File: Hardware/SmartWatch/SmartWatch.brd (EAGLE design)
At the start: 36.8 x 40.6 mm, 79 parts, among them U1 STM32L476, U10 MICRO-USB, U11 BNO055, U3 UG-2828GDEDF11, U4 FAN5331SX, U5 APDS-9960, U6 MCP73831, U7 AP2112K-3.3TRG-1, U8 ASDK-32.768, U9 ASCO-8

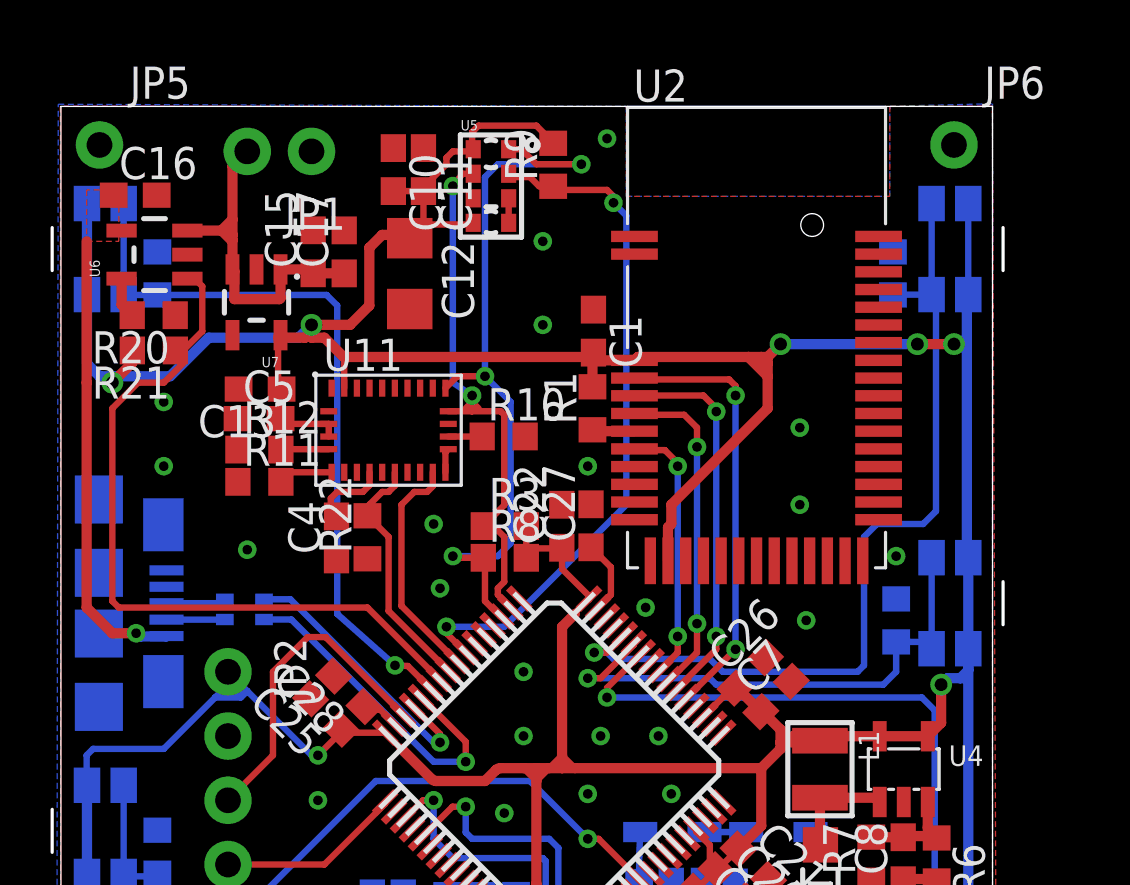
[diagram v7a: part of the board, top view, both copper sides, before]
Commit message: added test points and icreased keepout around bluetooth
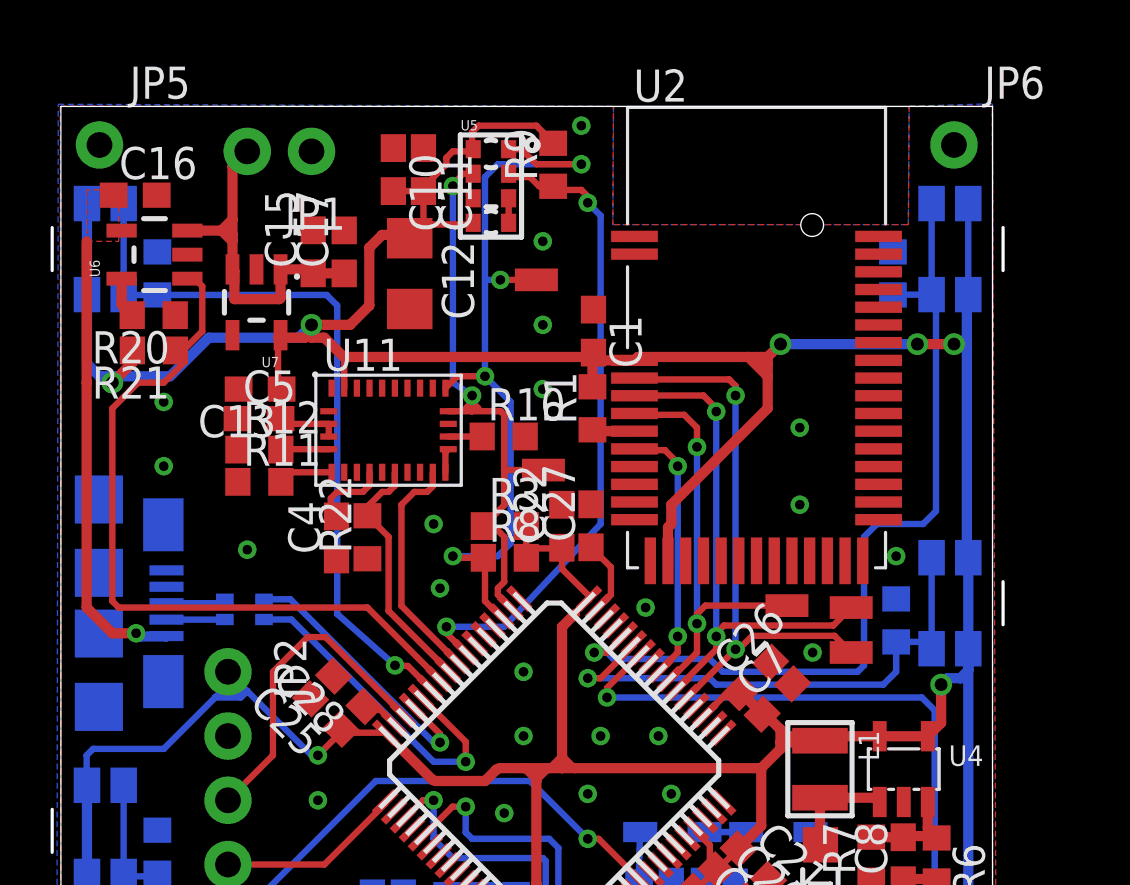
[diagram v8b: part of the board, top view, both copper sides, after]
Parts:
- added T1, T2, T3, T4, T5: TESTPOINT-0603, SmartWatch:TESTPOINT-0603
- moved C26 0.27 mm to (27.5, 18.1)
- moved C7 0.11 mm to (28.3, 17.2)
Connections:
- net BT_MISO: now also T5.1
- net BT_MOSI: now also T4.1
- net BT_SCK: now also T3.1
- net SCL: now also T2.1
- net SDA: now also T1.1
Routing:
- net BT_MISO: track 15.1 -> 21.0 mm
- net BT_SCK: track 17.2 -> 22.3 mm
- net BT_MOSI: track 13.1 -> 17.2 mm
- net SDA: track 30.2 -> 32.2 mm, vias 3 -> 4
- net SCL: track 22.5 -> 24.1 mm
- net G_INT: track 27.4 -> 25.8 mm
